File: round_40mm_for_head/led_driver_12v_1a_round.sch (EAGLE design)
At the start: 44 parts, among them IC1 LM2936MP-3.0, Q1 BSZ0902NSI, Q2 BSZ0902NSI, Q3 BSZ0902NSI, Q4 BSZ0902NSI, Q5 BSZ0902NSI, X1 87758-1016

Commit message: added adc resistors shutdown
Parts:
- removed IC1: LM2936MP-3.0, national-semiconductor:LM2936MP-3.0
- added C17: 100nF, resistor:C-EUC0402K
- added R12, R3: 10k, resistor:R-EU_R0402
- added R13: 10Meg, resistor:R-EU_R0402
- added T1: BCW-60B, transistor-neu-to92:BCW60-NPN-SOT23-BEC
- added U$3: TPS71550, TPS715:TPS715
- added U$5: SI1013, Si1013:SI1013
- C16: value 10uF -> 4.7uF
- R11: value 50m (Ohmite MCS1632R005FER) -> 5m (Ohmite MCS1632R005FER)
- R5: value 100k -> 110k
- R6: value 56.9k -> 10k
- R8: value 10m (Riedon CSR1206-0R001F1) -> 1m (Riedon CSR1206-0R001F1)
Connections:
- net N$11 renamed PA2
- net N$13 renamed PA3
- net N$16 renamed SCL
- net N$17 renamed MISO
- net N$18 renamed MOSI
- net N$20 renamed PB1
- net N$23 renamed PB2
- removed net N$22: U$2.PB3/RESET, X1-4.S
- removed net N$8: U$2.PA1/ADC1, X1-10.S
- new net N$24: R12.2, T1.B
- new net N$25: R3.2, T1.C, U$5.G
- new net N$27: C17.2, R5.1, U$5.D
- new net RESET: R12.1, R13.2, U$2.PB3/RESET, X1-4.S
- net +12V: now also R3.1, U$3.IN, U$5.S; no longer IC1.VIN, R5.1
- net DGND: now also R13.1, T1.E, U$3.GND, X1-10.S; no longer IC1.GND@1, IC1.GND@2
- net N$12: now also U$3.OUT; no longer IC1.VO
- net N$15: now also C17.1
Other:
- note removed: "The ESR, of the COUT capacitor must at least 300 mΩ, but no more than 8 Ω"
- note removed: "WARNING! SOLDER R8 TO GROUND MANUALLY!"
- moved on the sheet: X1-1, X1-10, X1-3, X1-4, X1-5, X1-6, X1-7, X1-8, X1-9

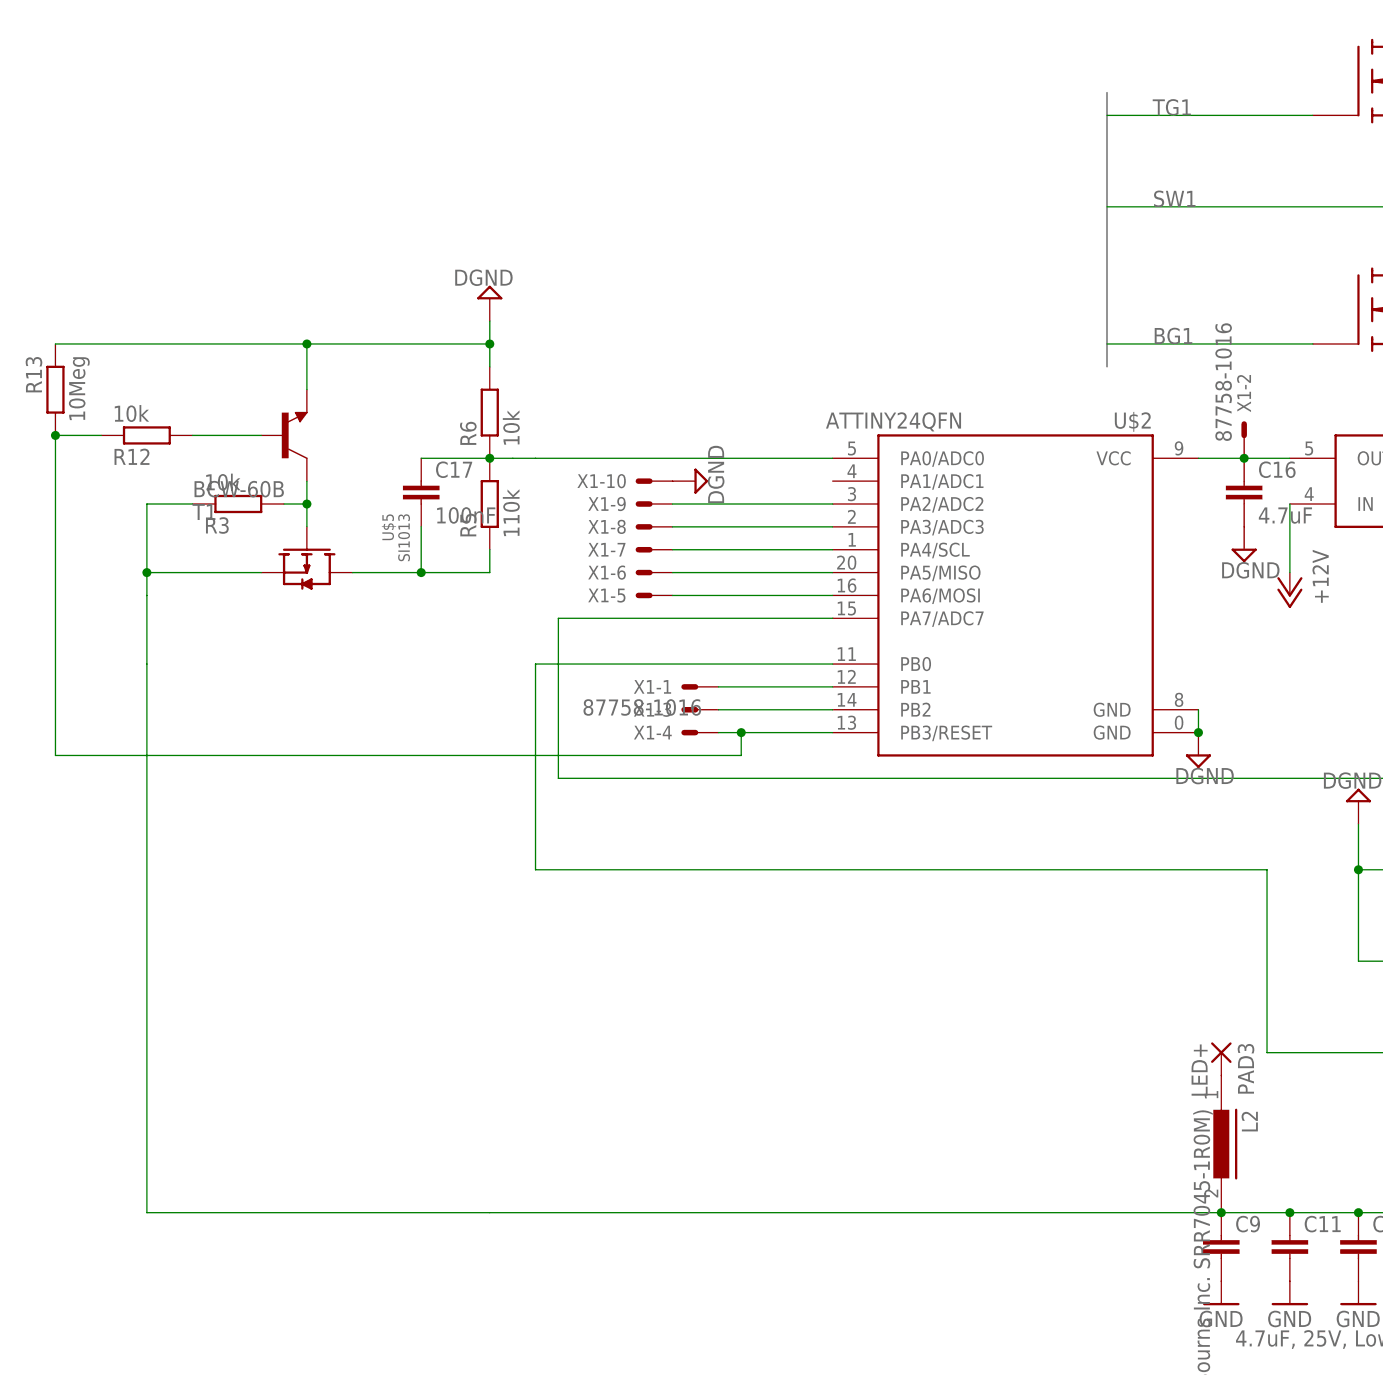
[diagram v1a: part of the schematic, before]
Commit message: added resistor to adc
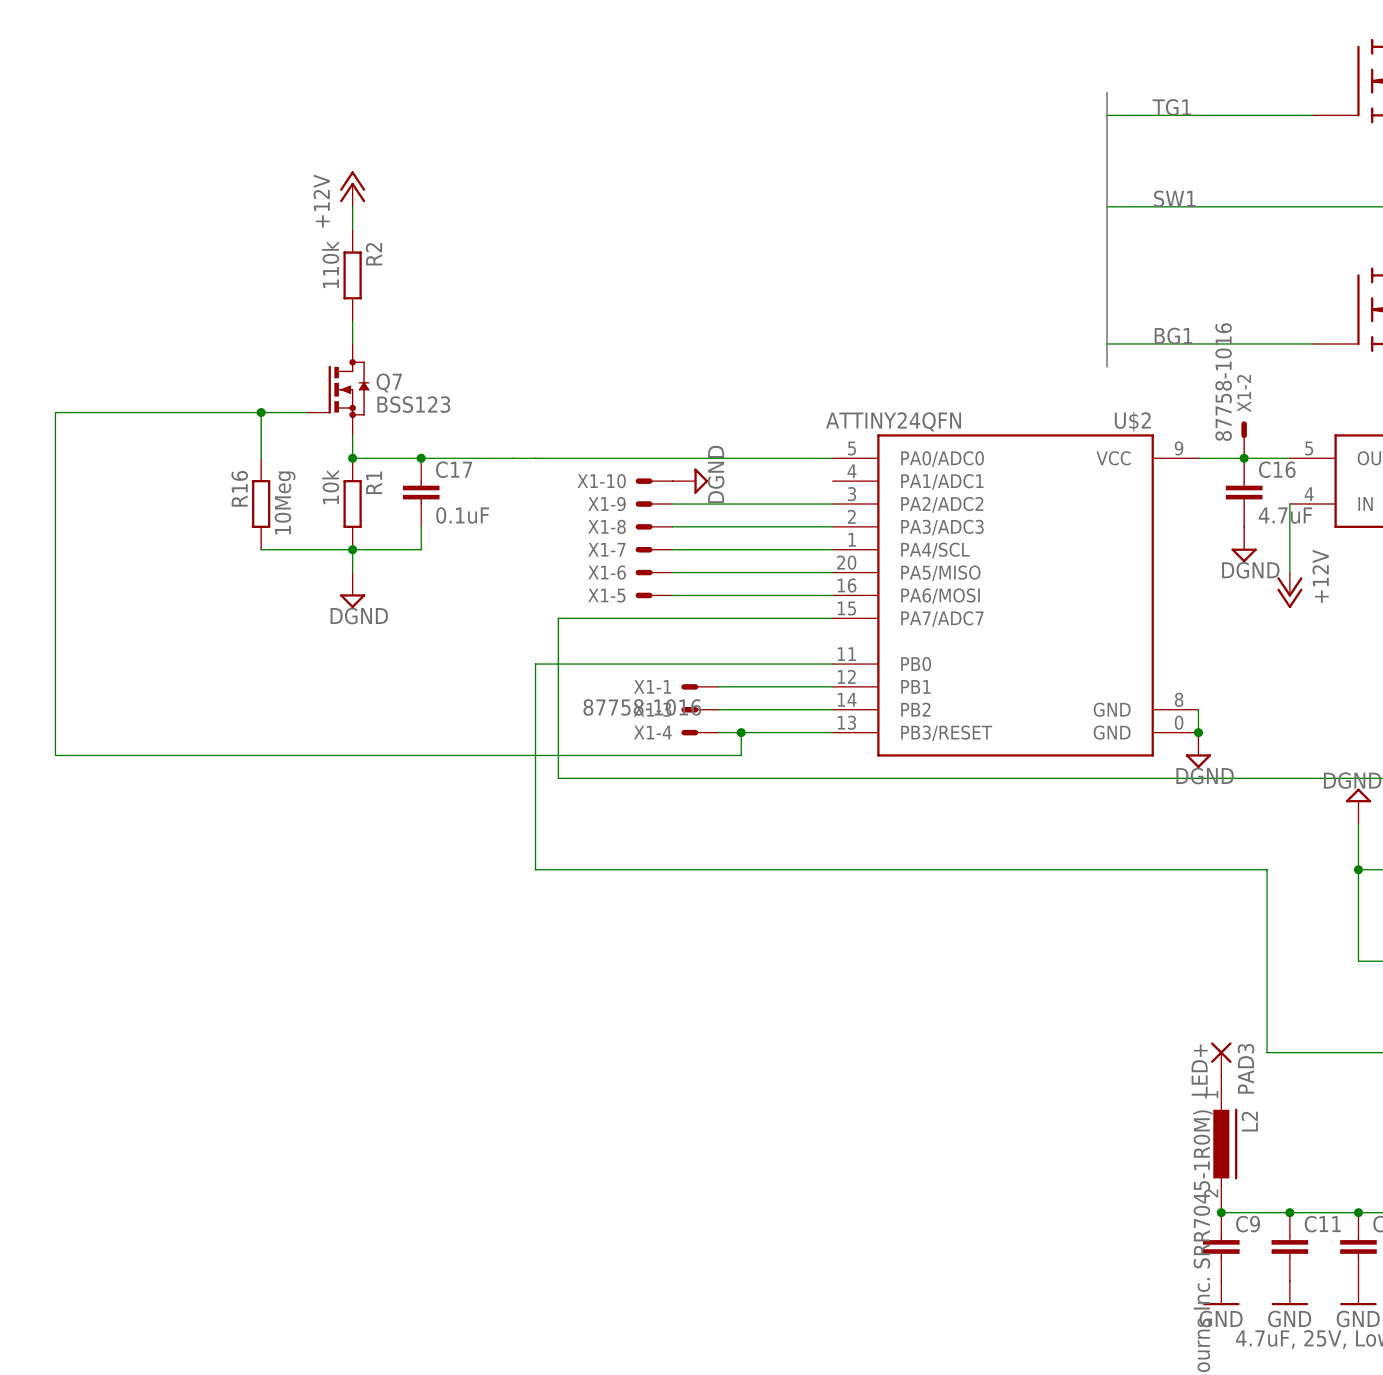
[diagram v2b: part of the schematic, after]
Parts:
- removed R12, R3, R6: 10k, resistor:R-EU_R0402
- removed R13: 10Meg, resistor:R-EU_R0402
- removed R5: 110k, resistor:R-EU_R0402
- removed T1: BCW-60B, transistor-neu-to92:BCW60-NPN-SOT23-BEC
- removed U$5: SI1013, Si1013:SI1013
- added Q7: BSS123, transistor-small-signal:BSS123
- added R1: 10k, resistor:R-EU_R0402
- added R16: 10Meg, resistor:R-EU_R0402
- added R2: 110k, resistor:R-EU_R0402
- C17: value 100nF -> 0.1uF
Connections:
- removed net N$24: R12.2, T1.B
- removed net N$25: R3.2, T1.C, U$5.G
- removed net N$27: C17.2, R5.1, U$5.D
- new net N$8: Q7.D, R2.2
- net +12V: now also R2.1; no longer R3.1, U$5.S
- net DGND: now also C17.2, R1.2, R16.2; no longer R13.1, R6.2, T1.E
- net N$15: now also Q7.S, R1.1; no longer R5.2, R6.1
- net RESET: now also Q7.G, R16.1; no longer R12.1, R13.2
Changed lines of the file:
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@@
 <part name="U$2" library="SparkFun-DigitalIC" deviceset="ATTINY24" device="QFN"/>
 <part name="SUPPLY8" library="supply2" deviceset="DGND" device=""/>
-<part name="R5" library="resistor" deviceset="R-EU_" device="R0402" value="110k"/>
-<part name="R6" library="resistor" deviceset="R-EU_" device="R0402" value="10k"/>
-<part name="SUPPLY10" library="supply2" deviceset="DGND" device=""/>
 <part name="C16" library="rcl" deviceset="C-EU" device="C1206" value="4.7uF"/>
 <part name="SUPPLY11" library="supply2" deviceset="DGND" device=""/>
@@
 <part name="GND3" library="supply1" deviceset="GND" device=""/>
 <part name="U$3" library="TPS715" deviceset="TPS715" device="" value="TPS71550"/>
-<part name="T1" library="transistor-neu-to92" deviceset="*-NPN-" device="SOT23-BEC" technology="BCW60" value="BCW-60B"/>
-<part name="U$5" library="Si1013" deviceset="SI1013" device=""/>
-<part name="R3" library="resistor" deviceset="R-EU_" device="R0402" value="10k"/>
-<part name="R12" library="resistor" deviceset="R-EU_" device="R0402" value="10k"/>
-<part name="R13" library="resistor" deviceset="R-EU_" device="R0402" value="10Meg"/>
 <part name="P+6" library="supply1" deviceset="+12V" device=""/>
 <part name="SUPPLY6" library="supply2" deviceset="DGND" device=""/>
 <part name="SUPPLY9" library="supply2" deviceset="DGND" device=""/>
-<part name="C17" library="resistor" deviceset="C-EU" device="C0402K" value="100nF"/>
+<part name="R1" library="resistor" deviceset="R-EU_" device="R0402" value="10k"/>
+<part name="R2" library="resistor" deviceset="R-EU_" device="R0402" value="110k"/>
+<part name="SUPPLY12" library="supply2" deviceset="DGND" device=""/>
+<part name="P+5" library="supply1" deviceset="+12V" device=""/>
+<part name="Q7" library="transistor-small-signal" deviceset="BSS123" device=""/>
+<part name="R16" library="resistor" deviceset="R-EU_" device="R0402" value="10Meg"/>
+<part name="C17" library="resistor" deviceset="C-EU" device="C0402K" value="0.1uF"/>
 </parts>
 <sheets>
@@
 <instance part="U$2" gate="G$1" x="-93.98" y="20.32" rot="MR0"/>
 <instance part="SUPPLY8" gate="G$1" x="-73.66" y="2.54"/>
-<instance part="R5" gate="G$1" x="-152.4" y="30.48" rot="R90"/>
-<instance part="R6" gate="G$1" x="-152.4" y="40.64" rot="R90"/>
-<instance part="SUPPLY10" gate="G$1" x="-152.4" y="53.34" rot="R180"/>
 <instance part="C16" gate="G$1" x="-68.58" y="33.02"/>
 <instance part="SUPPLY11" gate="G$1" x="-68.58" y="25.4"/>
@@
 <instance part="GND3" gate="1" x="63.5" y="-25.4" rot="MR0"/>
 <instance part="U$3" gate="G$1" x="-48.26" y="33.02" rot="MR0"/>
-<instance part="T1" gate="G$1" x="-175.26" y="38.1" rot="MR180"/>
-<instance part="U$5" gate="G$1" x="-172.72" y="22.86" rot="R270"/>
-<instance part="R3" gate="G$1" x="-180.34" y="30.48" rot="MR180"/>
-<instance part="R12" gate="G$1" x="-190.5" y="38.1" rot="MR180"/>
-<instance part="R13" gate="G$1" x="-200.66" y="43.18" rot="MR270"/>
 <instance part="P+6" gate="1" x="-63.5" y="20.32" rot="R180"/>
 <instance part="SUPPLY6" gate="G$1" x="-33.02" y="33.02" rot="MR270"/>
 <instance part="SUPPLY9" gate="G$1" x="-129.54" y="33.02" rot="R90"/>
+<instance part="R1" gate="G$1" x="-167.64" y="30.48" rot="R270"/>
+<instance part="R2" gate="G$1" x="-167.64" y="55.88" rot="R270"/>
+<instance part="SUPPLY12" gate="G$1" x="-167.64" y="20.32"/>
+<instance part="P+5" gate="1" x="-167.64" y="66.04"/>
+<instance part="Q7" gate="G$1" x="-167.64" y="43.18"/>
+<instance part="R16" gate="G$1" x="-177.8" y="30.48" rot="MR270"/>
 <instance part="C17" gate="G$1" x="-160.02" y="33.02"/>
 </instances>
@@
 <pinref part="P+1" gate="1" pin="+12V"/>
 <junction x="-48.26" y="-48.26"/>
-<wire x1="-71.12" y1="-48.26" x2="-152.4" y2="-48.26" width="0.1524" layer="91"/>
-<pinref part="U$5" gate="G$1" pin="S"/>
-<wire x1="-177.8" y1="22.86" x2="-190.5" y2="22.86" width="0.1524" layer="91"/>
-<wire x1="-190.5" y1="22.86" x2="-190.5" y2="30.48" width="0.1524" layer="91"/>
-<pinref part="R3" gate="G$1" pin="1"/>
-<wire x1="-190.5" y1="30.48" x2="-185.42" y2="30.48" width="0.1524" layer="91"/>
-<wire x1="-190.5" y1="22.86" x2="-190.5" y2="20.32" width="0.1524" layer="91"/>
-<wire x1="-190.5" y1="20.32" x2="-190.5" y2="12.7" width="0.1524" layer="91"/>
-<junction x="-190.5" y="22.86"/>
-<wire x1="-152.4" y1="-48.26" x2="-190.5" y2="-48.26" width="0.1524" layer="91"/>
-<wire x1="-190.5" y1="-48.26" x2="-190.5" y2="12.7" width="0.1524" layer="91"/>
 </segment>
 <segment>
@@
 <pinref part="P+6" gate="1" pin="+12V"/>
 <wire x1="-63.5" y1="22.86" x2="-63.5" y2="30.48" width="0.1524" layer="91"/>
+</segment>
+<segment>
+<pinref part="P+5" gate="1" pin="+12V"/>
+<pinref part="R2" gate="G$1" pin="1"/>
+<wire x1="-167.64" y1="60.96" x2="-167.64" y2="63.5" width="0.1524" layer="91"/>
 </segment>
 </net>
@@
 </segment>
 <segment>
-<pinref part="R6" gate="G$1" pin="2"/>
-<pinref part="SUPPLY10" gate="G$1" pin="DGND"/>
-<wire x1="-152.4" y1="50.8" x2="-152.4" y2="48.26" width="0.1524" layer="91"/>
-<pinref part="R13" gate="G$1" pin="1"/>
-<pinref part="T1" gate="G$1" pin="E"/>
-<wire x1="-152.4" y1="48.26" x2="-152.4" y2="45.72" width="0.1524" layer="91"/>
-<wire x1="-200.66" y1="48.26" x2="-172.72" y2="48.26" width="0.1524" layer="91"/>
-<wire x1="-172.72" y1="48.26" x2="-172.72" y2="43.18" width="0.1524" layer="91"/>
-<wire x1="-172.72" y1="48.26" x2="-152.4" y2="48.26" width="0.1524" layer="91"/>
-<junction x="-172.72" y="48.26"/>
-<junction x="-152.4" y="48.26"/>
-</segment>
-<segment>
 <pinref part="C16" gate="G$1" pin="2"/>
 <pinref part="SUPPLY11" gate="G$1" pin="DGND"/>
@@
 <pinref part="X1" gate="-10" pin="S"/>
 <pinref part="SUPPLY9" gate="G$1" pin="DGND"/>
+</segment>
+<segment>
+<pinref part="SUPPLY12" gate="G$1" pin="DGND"/>
+<pinref part="R1" gate="G$1" pin="2"/>
+<wire x1="-167.64" y1="22.86" x2="-167.64" y2="25.4" width="0.1524" layer="91"/>
+<pinref part="R16" gate="G$1" pin="2"/>
+<wire x1="-167.64" y1="25.4" x2="-177.8" y2="25.4" width="0.1524" layer="91"/>
+<junction x="-167.64" y="25.4"/>
+<pinref part="C17" gate="G$1" pin="2"/>
+<wire x1="-167.64" y1="25.4" x2="-160.02" y2="25.4" width="0.1524" layer="91"/>
+<wire x1="-160.02" y1="25.4" x2="-160.02" y2="27.94" width="0.1524" layer="91"/>
 </segment>
 </net>
@@
 <net name="N$15" class="0">
 <segment>
-<pinref part="R6" gate="G$1" pin="1"/>
-<pinref part="R5" gate="G$1" pin="2"/>
 <wire x1="-152.4" y1="35.56" x2="-149.86" y2="35.56" width="0.1524" layer="91"/>
 <wire x1="-149.86" y1="35.56" x2="-147.32" y2="35.56" width="0.1524" layer="91"/>
-<junction x="-152.4" y="35.56"/>
 <pinref part="U$2" gate="G$1" pin="PA0/ADC0"/>
 <wire x1="-147.32" y1="35.56" x2="-114.3" y2="35.56" width="0.1524" layer="91"/>
+<pinref part="Q7" gate="G$1" pin="S"/>
+<pinref part="R1" gate="G$1" pin="1"/>
+<wire x1="-167.64" y1="38.1" x2="-167.64" y2="35.56" width="0.1524" layer="91"/>
+<wire x1="-152.4" y1="35.56" x2="-160.02" y2="35.56" width="0.1524" layer="91"/>
+<junction x="-167.64" y="35.56"/>
 <pinref part="C17" gate="G$1" pin="1"/>
-<wire x1="-152.4" y1="35.56" x2="-160.02" y2="35.56" width="0.1524" layer="91"/>
+<wire x1="-160.02" y1="35.56" x2="-167.64" y2="35.56" width="0.1524" layer="91"/>
+<junction x="-160.02" y="35.56"/>
 </segment>
 </net>
@@
 <wire x1="-124.46" y1="5.08" x2="-124.46" y2="2.54" width="0.1524" layer="91"/>
 <junction x="-124.46" y="5.08"/>
-<pinref part="R12" gate="G$1" pin="1"/>
-<pinref part="R13" gate="G$1" pin="2"/>
-<wire x1="-200.66" y1="38.1" x2="-195.58" y2="38.1" width="0.1524" layer="91"/>
 <wire x1="-124.46" y1="2.54" x2="-200.66" y2="2.54" width="0.1524" layer="91"/>
 <wire x1="-200.66" y1="2.54" x2="-200.66" y2="38.1" width="0.1524" layer="91"/>
-<junction x="-200.66" y="38.1"/>
+<pinref part="Q7" gate="G$1" pin="G"/>
+<pinref part="R16" gate="G$1" pin="1"/>
+<wire x1="-172.72" y1="40.64" x2="-177.8" y2="40.64" width="0.1524" layer="91"/>
+<wire x1="-177.8" y1="40.64" x2="-177.8" y2="35.56" width="0.1524" layer="91"/>
+<wire x1="-177.8" y1="40.64" x2="-200.66" y2="40.64" width="0.1524" layer="91"/>
+<wire x1="-200.66" y1="40.64" x2="-200.66" y2="38.1" width="0.1524" layer="91"/>
+<junction x="-177.8" y="40.64"/>
 </segment>
 </net>
@@
 </segment>
 </net>
-<net name="N$24" class="0">
-<segment>
-<pinref part="R12" gate="G$1" pin="2"/>
-<pinref part="T1" gate="G$1" pin="B"/>
-<wire x1="-177.8" y1="38.1" x2="-185.42" y2="38.1" width="0.1524" layer="91"/>
-</segment>
-</net>
-<net name="N$25" class="0">
-<segment>
-<pinref part="U$5" gate="G$1" pin="G"/>
-<pinref part="T1" gate="G$1" pin="C"/>
-<wire x1="-172.72" y1="33.02" x2="-172.72" y2="30.48" width="0.1524" layer="91"/>
-<pinref part="R3" gate="G$1" pin="2"/>
-<wire x1="-172.72" y1="30.48" x2="-172.72" y2="27.94" width="0.1524" layer="91"/>
-<wire x1="-175.26" y1="30.48" x2="-172.72" y2="30.48" width="0.1524" layer="91"/>
-<junction x="-172.72" y="30.48"/>
-</segment>
-</net>
-<net name="N$27" class="0">
-<segment>
-<pinref part="R5" gate="G$1" pin="1"/>
-<pinref part="U$5" gate="G$1" pin="D"/>
-<wire x1="-167.64" y1="22.86" x2="-160.02" y2="22.86" width="0.1524" layer="91"/>
-<wire x1="-160.02" y1="22.86" x2="-152.4" y2="22.86" width="0.1524" layer="91"/>
-<wire x1="-152.4" y1="22.86" x2="-152.4" y2="25.4" width="0.1524" layer="91"/>
-<pinref part="C17" gate="G$1" pin="2"/>
-<wire x1="-160.02" y1="27.94" x2="-160.02" y2="22.86" width="0.1524" layer="91"/>
-<junction x="-160.02" y="22.86"/>
-</segment>
-</net>
+<net name="N$8" class="0">
+<segment>
+<pinref part="R2" gate="G$1" pin="2"/>
+<pinref part="Q7" gate="G$1" pin="D"/>
+<wire x1="-167.64" y1="50.8" x2="-167.64" y2="48.26" width="0.1524" layer="91"/>
+</segment>
+</net>
